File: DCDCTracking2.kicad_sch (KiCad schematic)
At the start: 30 parts, among them Q501 MMBT3906, U501 LT8612

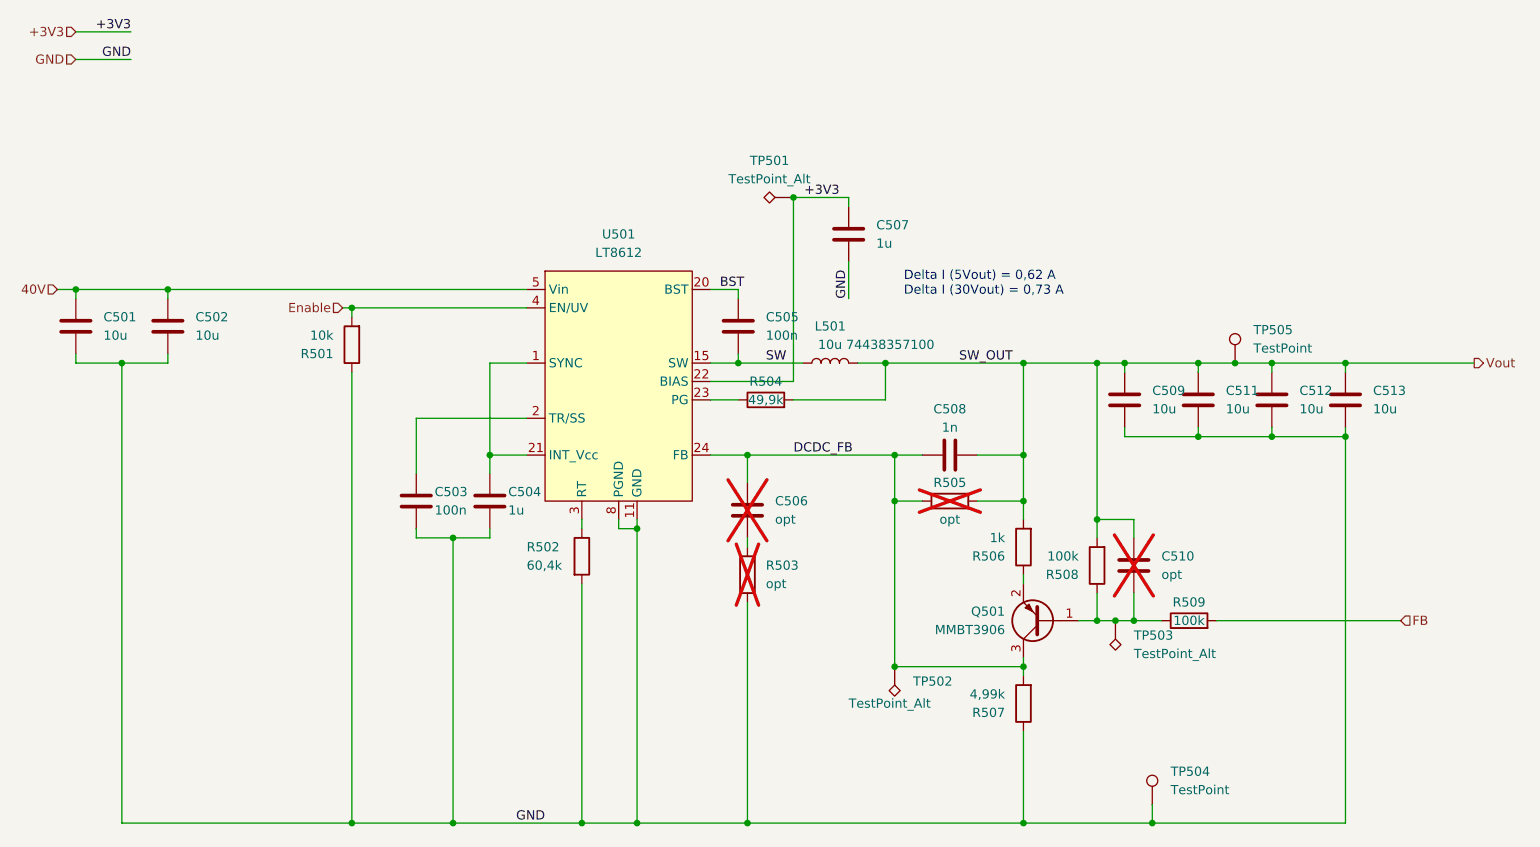
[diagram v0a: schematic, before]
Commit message: added Ch2 and removed global power flags
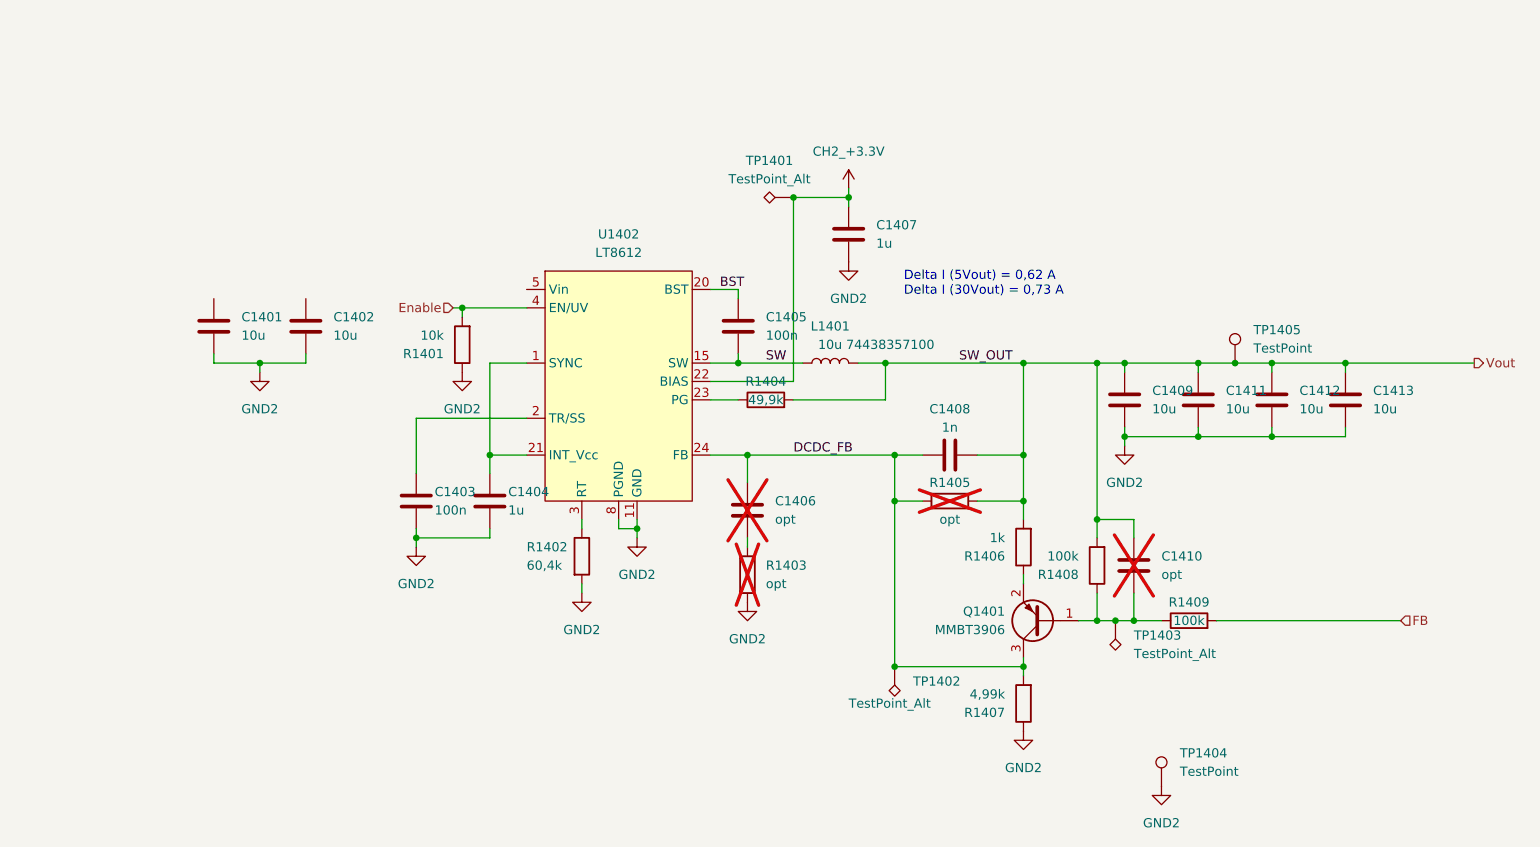
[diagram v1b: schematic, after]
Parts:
- removed C501, C502, C509, C511, C512, C513: 10u, Capacitor_SMD:C_1206_3216Metric, symbol Device:C
- removed C503, C505: 100n, Capacitor_SMD:C_0603_1608Metric, symbol Device:C
- removed C504, C507: 1u, Capacitor_SMD:C_0603_1608Metric, symbol Device:C
- removed C506, C510: opt, Capacitor_SMD:C_0603_1608Metric, symbol Device:C
- removed C508: 1n, Capacitor_SMD:C_0603_1608Metric, symbol Device:C
- removed L501: 10u 74438357100, Inductor_SMD:L_Wuerth_MAPI-4030, symbol Device:L
- removed Q501: MMBT3906, Package_TO_SOT_SMD:SOT-23-3, symbol Transistor_BJT:MMBT3906
- removed R501: 10k, Resistor_SMD:R_0603_1608Metric, symbol Device:R
- removed R502: 60,4k, Resistor_SMD:R_0603_1608Metric, symbol Device:R
- removed R503, R505: opt, Resistor_SMD:R_0603_1608Metric, symbol Device:R
- removed R504: 49,9k, Resistor_SMD:R_0603_1608Metric, symbol Device:R
- removed R506: 1k, Resistor_SMD:R_0603_1608Metric, symbol Device:R
- removed R507: 4,99k, Resistor_SMD:R_0603_1608Metric, symbol Device:R
- removed R508, R509: 100k, Resistor_SMD:R_0603_1608Metric, symbol Device:R
- removed TP501, TP502, TP503: TestPoint_Alt, TestPoint:TestPoint_Pad_D1.0mm, symbol Connector:TestPoint_Alt
- removed TP504, TP505: TestPoint, LibEigen:SMD Test Point PCWCTE, symbol Connector:TestPoint
- removed U501: LT8612, Package_DFN_QFN:QFN-28-1EP_3x6mm_P0.5mm_EP1.7x4.75mm_ThermalVias, symbol eiene Symbole:LT8612
- added C1401, C1402, C1409, C1411, C1412, C1413: 10u, Capacitor_SMD:C_1206_3216Metric, symbol Device:C
- added C1403, C1405: 100n, Capacitor_SMD:C_0603_1608Metric, symbol Device:C
- added C1404, C1407: 1u, Capacitor_SMD:C_0603_1608Metric, symbol Device:C
- added C1406, C1410: opt, Capacitor_SMD:C_0603_1608Metric, symbol Device:C
- added C1408: 1n, Capacitor_SMD:C_0603_1608Metric, symbol Device:C
- added L1401: 10u 74438357100, Inductor_SMD:L_Wuerth_MAPI-4030, symbol Device:L
- added Q1401: MMBT3906, Package_TO_SOT_SMD:SOT-23-3, symbol Transistor_BJT:MMBT3906
- added R1401: 10k, Resistor_SMD:R_0603_1608Metric, symbol Device:R
- added R1402: 60,4k, Resistor_SMD:R_0603_1608Metric, symbol Device:R
- added R1403, R1405: opt, Resistor_SMD:R_0603_1608Metric, symbol Device:R
- added R1404: 49,9k, Resistor_SMD:R_0603_1608Metric, symbol Device:R
- added R1406: 1k, Resistor_SMD:R_0603_1608Metric, symbol Device:R
- added R1407: 4,99k, Resistor_SMD:R_0603_1608Metric, symbol Device:R
- added R1408, R1409: 100k, Resistor_SMD:R_0603_1608Metric, symbol Device:R
- added TP1401, TP1402, TP1403: TestPoint_Alt, TestPoint:TestPoint_Pad_D1.0mm, symbol Connector:TestPoint_Alt
- added TP1404, TP1405: TestPoint, LibEigen:SMD Test Point PCWCTE, symbol Connector:TestPoint
- added U1402: LT8612, Package_DFN_QFN:QFN-28-1EP_3x6mm_P0.5mm_EP1.7x4.75mm_ThermalVias, symbol eiene Symbole:LT8612
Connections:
- net BST: now also C1405.1, U1402.20 (BST)
- net DCDC_FB: now also C1406.1, C1408.1, Q1401.3 (C), R1405.1, R1407.2, TP1402.1, U1402.24 (FB)
- net Enable: now also R1401.2, U1402.4 (EN/UV)
- net FB: now also R1409.2
- net SW: now also C1405.2, L1401.1, U1402.15 (SW), U1402.16 (SW), U1402.17 (SW), U1402.18 (SW), U1402.19 (SW)
- net Vin: now also U1402.5 (Vin), U1402.6 (Vin), U1402.7 (Vin)
- net Vout: now also C1408.2, C1409.1, C1410.1, C1411.1, C1412.1, C1413.1, L1401.2, R1404.2, R1405.2, R1406.2, R1408.2, TP1405.1
- new net: C1404.1, U1402.1 (SYNC), U1402.21 (INT_Vcc)
- new net: C1410.2, Q1401.1 (B), R1408.1, R1409.1, TP1403.1
- new net: C1403.1, U1402.2 (TR/SS)
- new net: R1402.1, U1402.3 (RT)
- new net: Q1401.2 (E), R1406.1
- new net: R1404.1, U1402.23 (PG)
- new net: C1406.2, R1403.1
- new net CH2_+3.3V: C1407.1, TP1401.1, U1402.22 (BIAS)
- new net EP: C1401.2, C1402.2, C1403.2, C1404.2, C1407.2, C1409.2, C1411.2, C1412.2, C1413.2, R1401.1, R1402.2, R1403.2, R1407.1, TP1404.1, U1402.10 (PGND), U1402.11 (GND), U1402.12 (GND), U1402.13 (GND), U1402.14 (GND), U1402.29 (EP), U1402.8 (PGND), U1402.9 (PGND)
